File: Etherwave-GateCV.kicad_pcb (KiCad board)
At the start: 2 copper layers, 67 x 56.5 mm, 76 parts, among them J1 Etherwave Brd, J2 Volume CV, J3 Pitch CV, J4 Gate, Q1 PMP4501Y, Q2 PMBT3906, Q3 PMP4501Y, U1 LM13700, U2 CD4093, U3 CD4093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

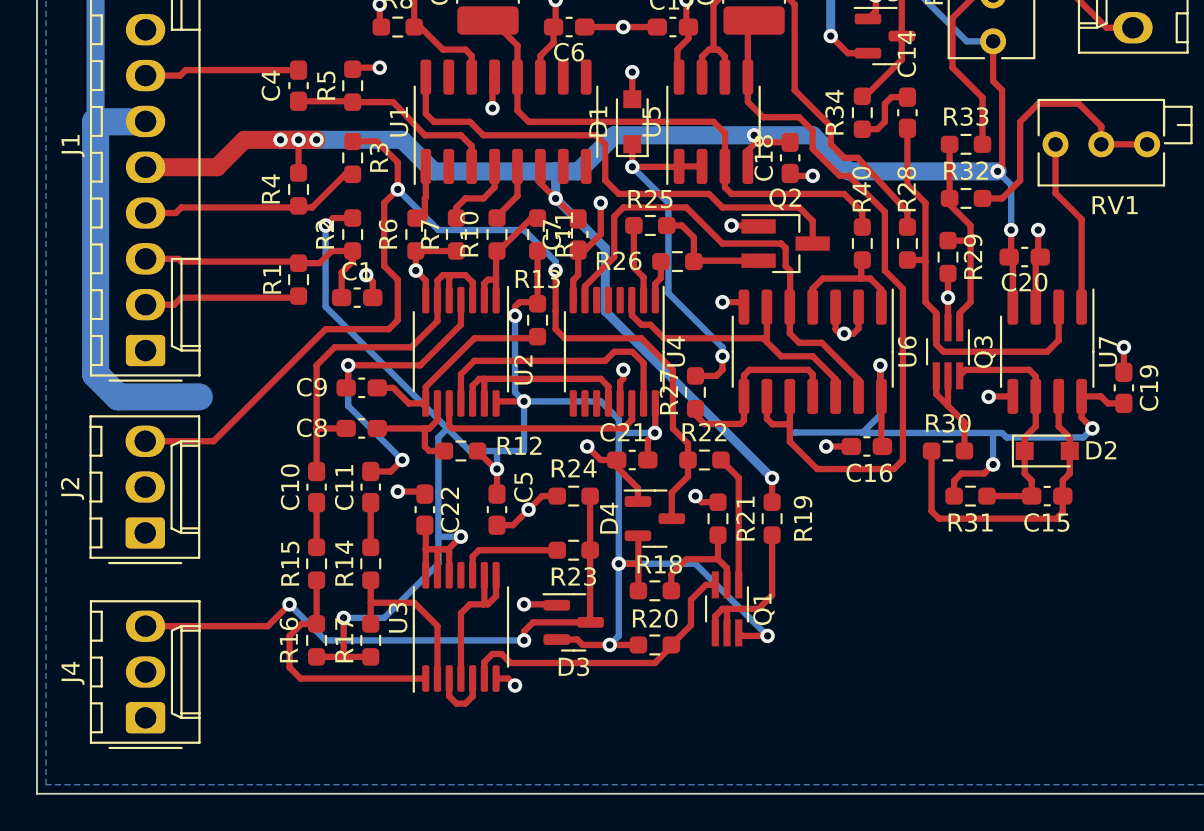
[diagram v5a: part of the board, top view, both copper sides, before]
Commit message: power routing completed
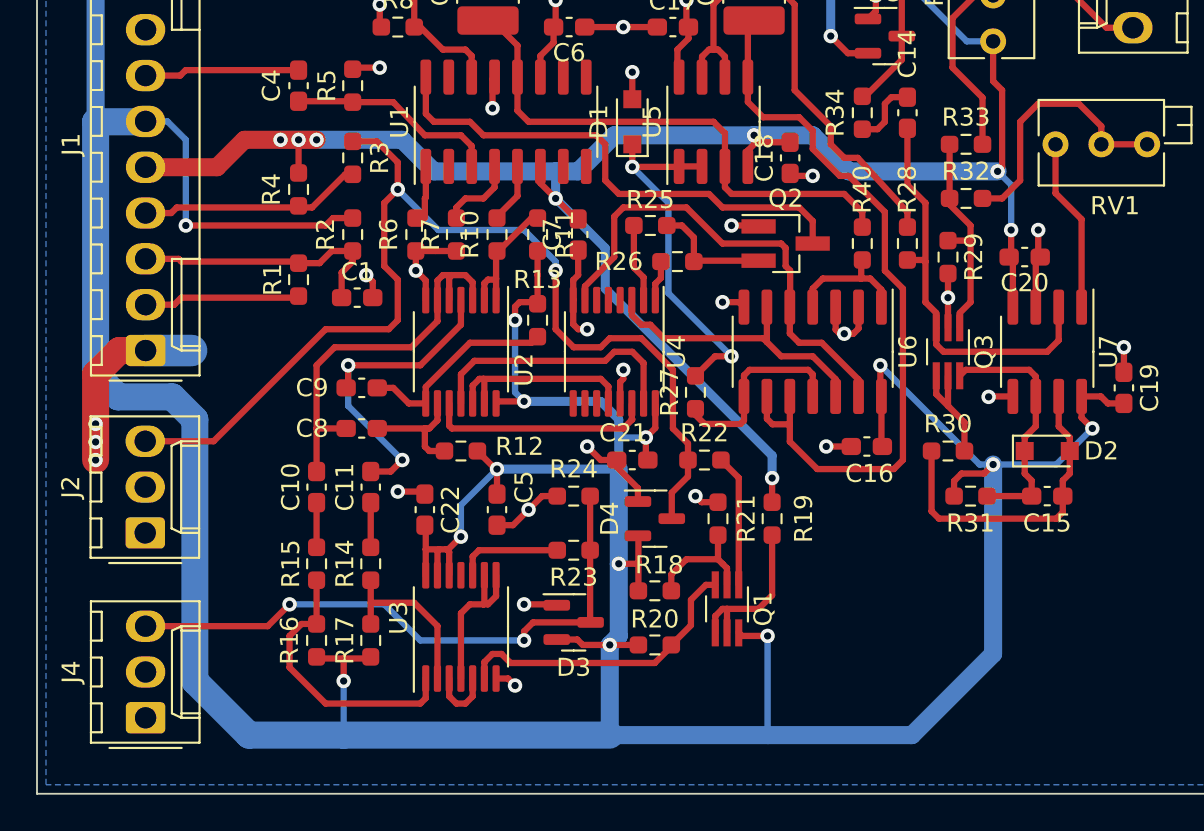
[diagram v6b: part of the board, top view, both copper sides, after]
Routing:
- net +12V: track 273.2 -> 328.6 mm
- net GND: track 60.3 -> 69.7 mm, vias 26 -> 29
- net Net-(R15-Pad1): track 13.8 -> 15.5 mm

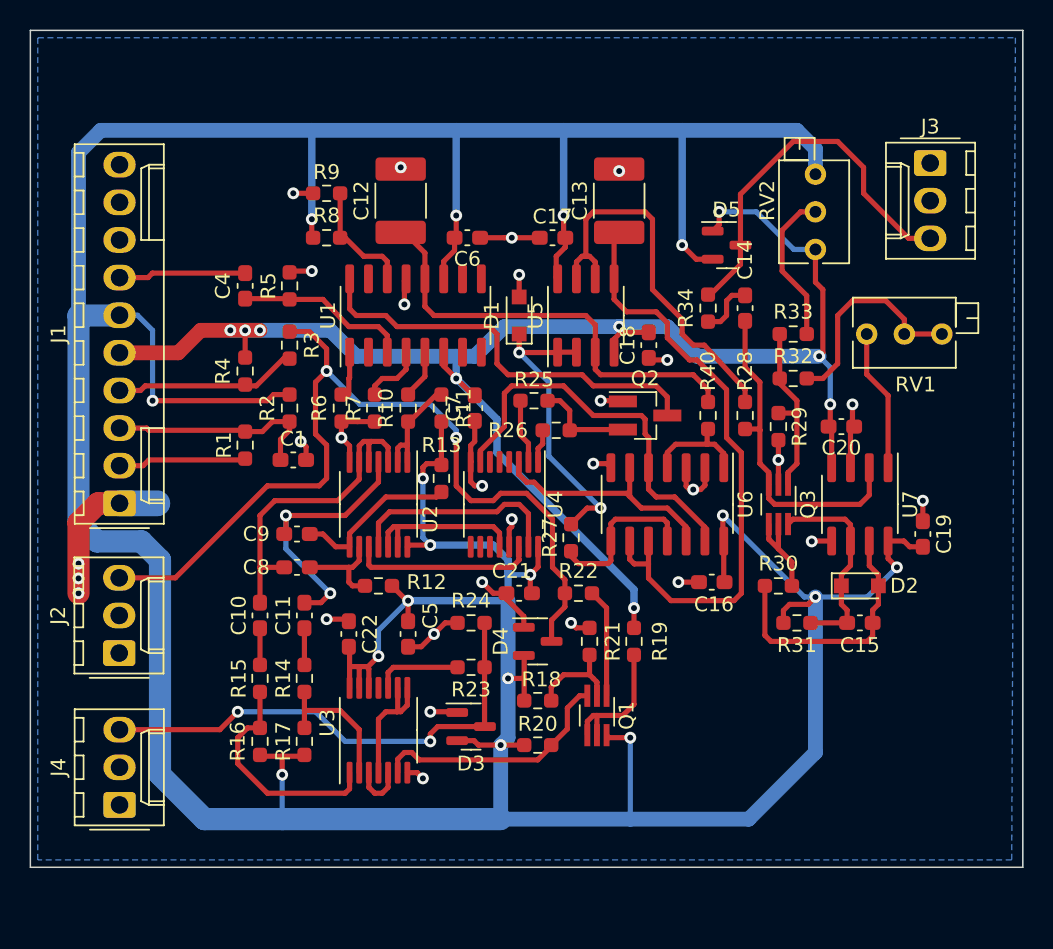
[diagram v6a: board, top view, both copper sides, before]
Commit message: silk screen done and mountiong holes placed
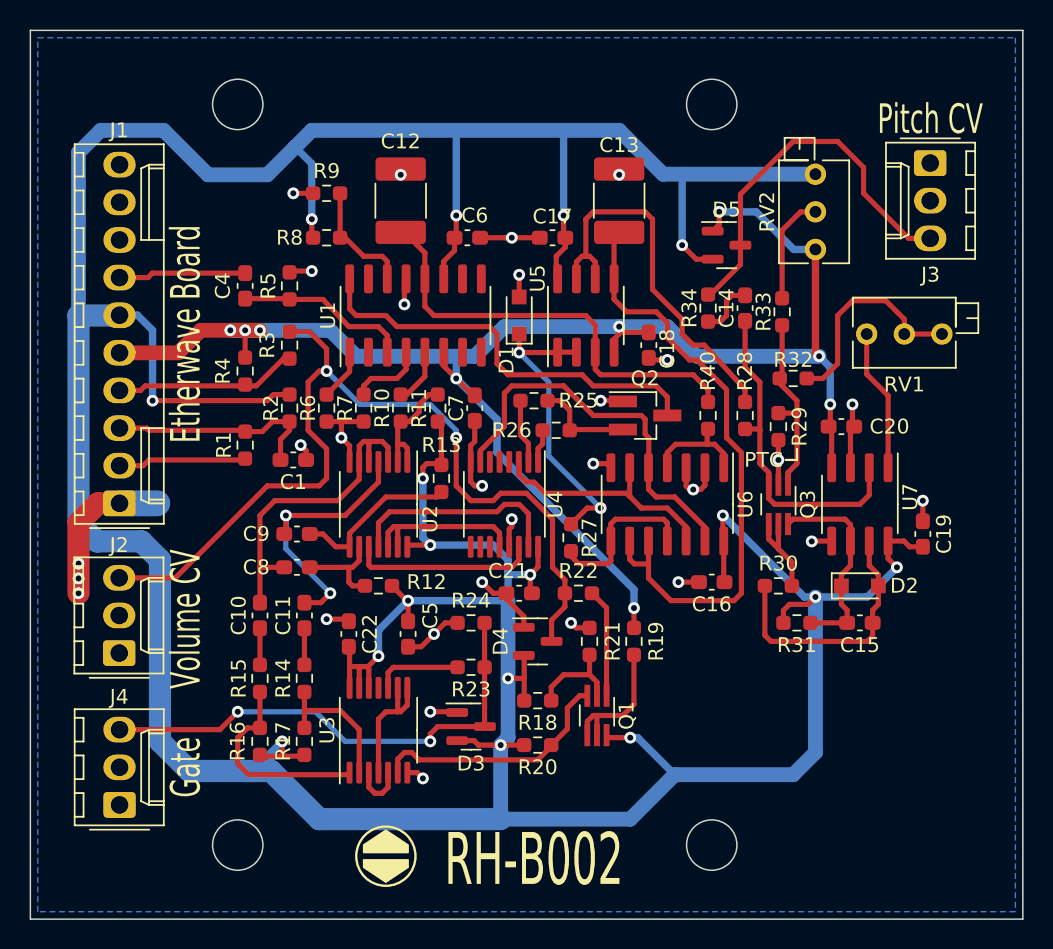
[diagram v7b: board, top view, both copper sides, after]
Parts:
- moved R33 1.68 mm to (104.8, 69.0), turned to -90 degrees
- moved R6 1.00 mm to (74.0, 75.5)
- moved R7 0.75 mm to (76.5, 75.5)
- moved R10 0.50 mm to (79.0, 75.5)
- moved R11 0.25 mm to (81.5, 75.5)
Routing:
- net +12V: track 328.6 -> 322.8 mm
- net Net-(R33-Pad1): track 10.5 -> 7.36 mm
- net Net-(R15-Pad1): track 15.5 -> 13.9 mm
- net Net-(R10-Pad2): track 7.44 -> 8.39 mm
- net Net-(R7-Pad2): track 4.32 -> 5.07 mm
- net Net-(D4-Pad3): track 59.9 -> 60.6 mm
- net Net-(Q3-Pad1): track 12.2 -> 12.8 mm
- net Net-(R6-Pad1): track 2.89 -> 3.51 mm
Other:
- board size 67 x 56.5 mm -> 67 x 60 mm
- board text added: "Etherwave Board"
- board text added: "Gate"
- board text added: "PTC"
- board text added: "Pitch CV"
- board text added: "RH-B002"
- board text added: "Volume CV"

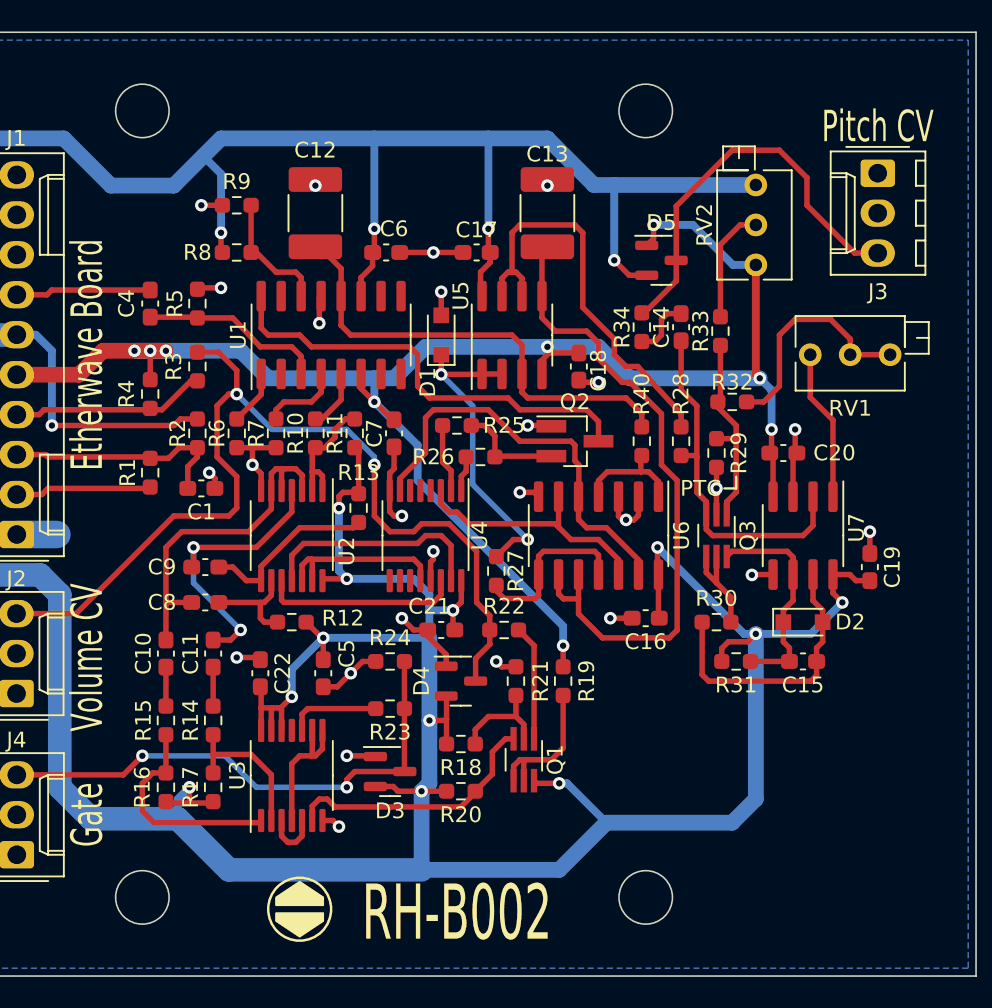
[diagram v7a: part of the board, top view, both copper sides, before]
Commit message: added mounting holes
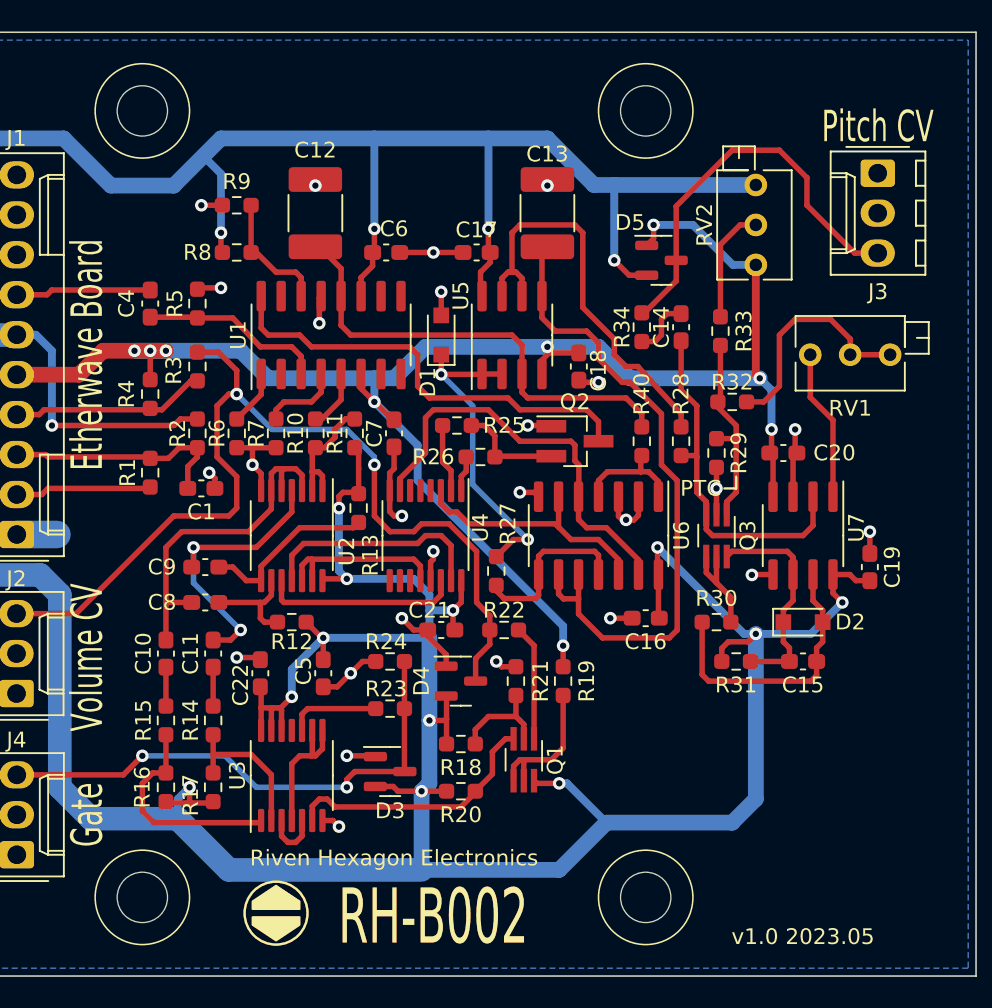
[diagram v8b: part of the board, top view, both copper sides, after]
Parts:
- added H1: MountingHole, MountingHole:MountingHole_3.2mm_M3_DIN965, F.Cu at (100.0, 55.0)
- added H2: MountingHole, MountingHole:MountingHole_3.2mm_M3_DIN965, F.Cu at (68.0, 55.0)
- added H3: MountingHole, MountingHole:MountingHole_3.2mm_M3_DIN965, F.Cu at (68.0, 105.0)
- added H4: MountingHole, MountingHole:MountingHole_3.2mm_M3_DIN965, F.Cu at (100.0, 105.0)
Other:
- outline, holes or cut-outs redrawn
- board text added: "Riven Hexagon Electronics"
- board text added: "v1.0 2023.05"
